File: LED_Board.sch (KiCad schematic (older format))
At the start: 26 parts, among them J1 Conn_01x06, J2 Conn_01x02, SW1 SW_Push, U1 PCA9531PW_LED_Driver_i2c

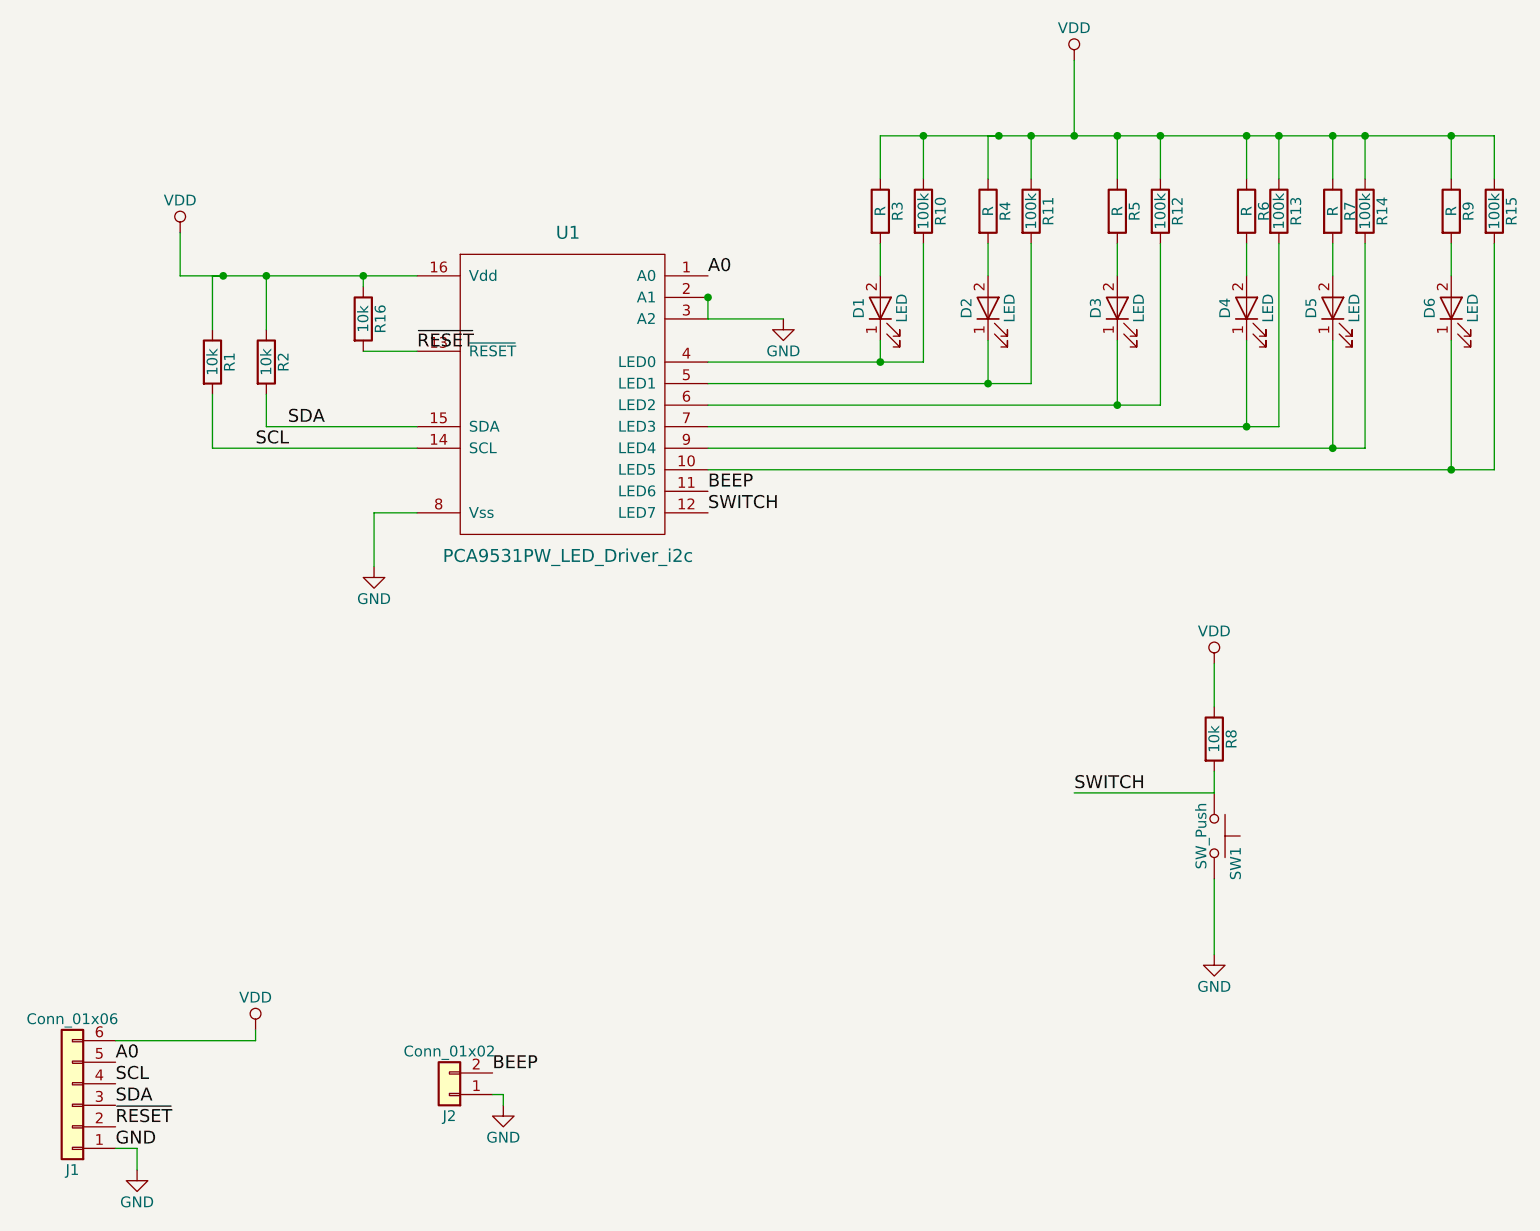
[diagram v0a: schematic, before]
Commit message: Arduino code able to read/write
Fixed a bug that stopped the code reading the status of the input pins.

Updated the PCB files based on the findings that I made during bring-up.
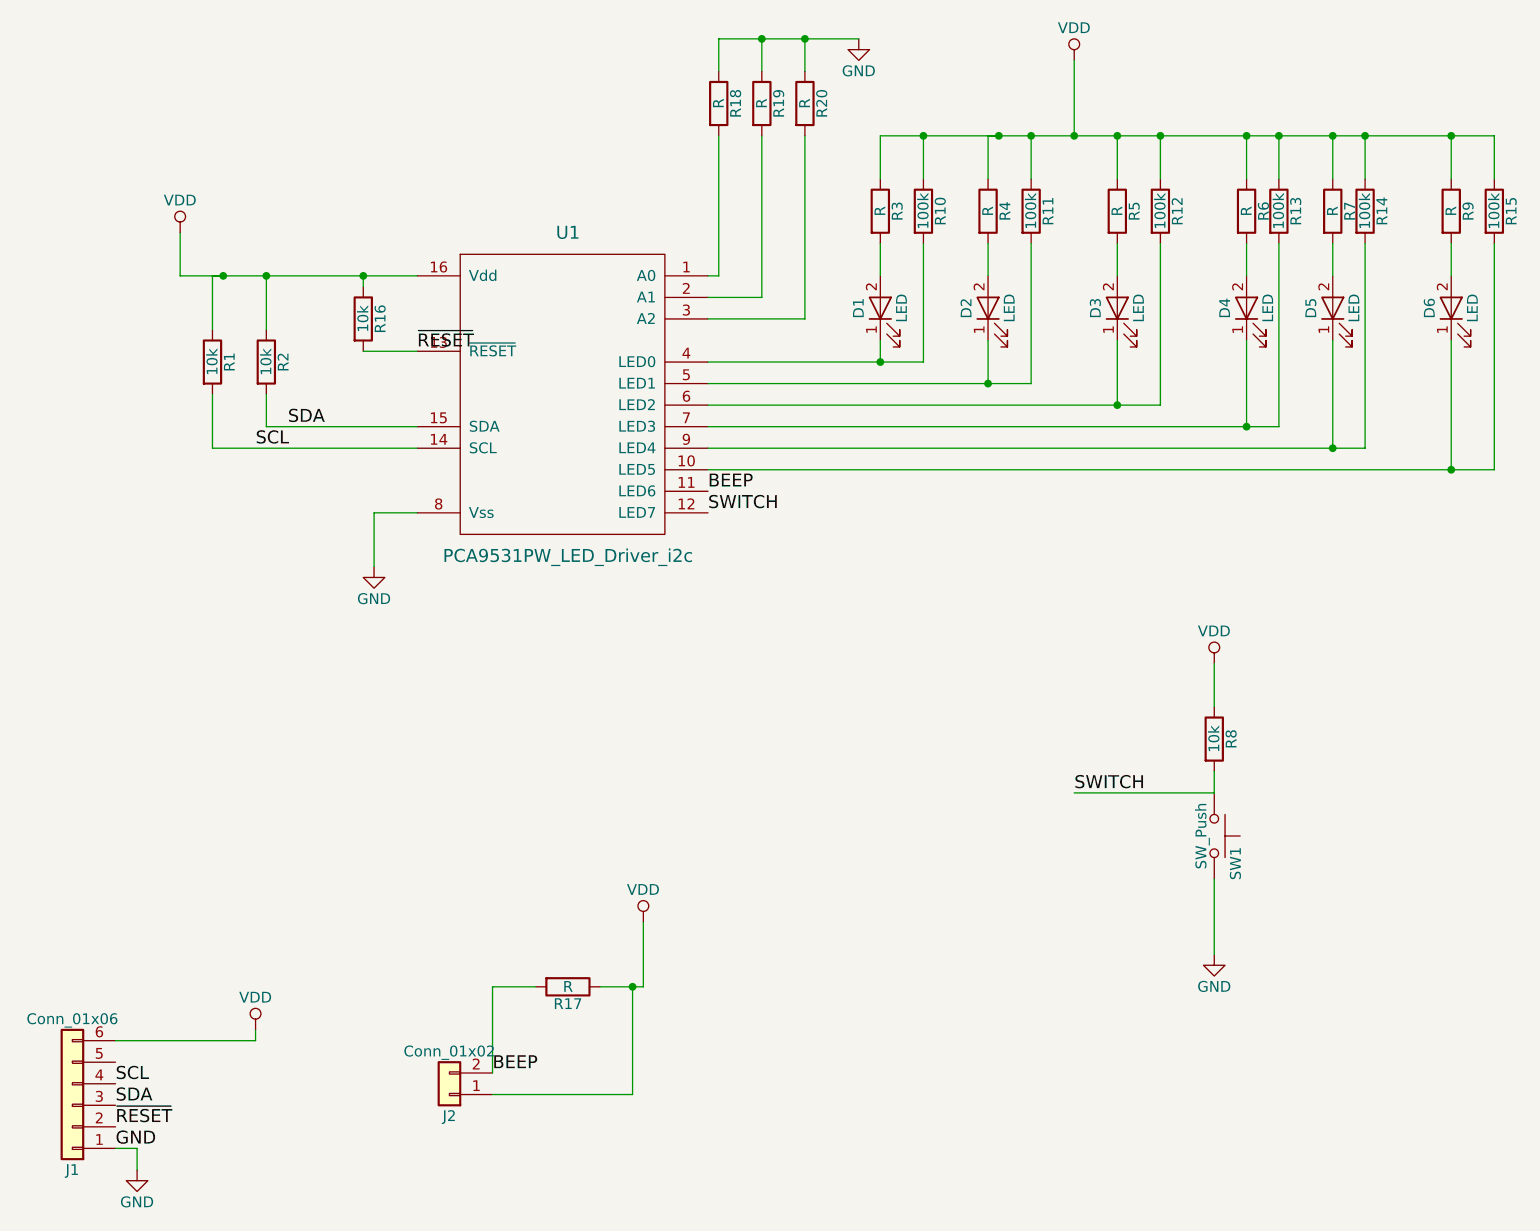
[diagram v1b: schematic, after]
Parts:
- added R17: R, Resistors_SMD:R_1206_HandSoldering, symbol R
- added R18, R19, R20: R, TJS-Kicad:R_1206_Jumper, symbol R
- SW1: footprint Buttons_Switches_THT:SW_TH_Tactile_Omron_B3F-10xx -> Buttons_Switches_THT:SW_PUSH_6mm
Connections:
- net BEEP: now also R17.2
- net GND: now also R18.1, R19.1, R20.1; no longer J2.1 (Pin_1), U1.2 (A1), U1.3 (A2)
- net VDD: now also J2.1 (Pin_1), R17.1
- net A0: no longer names the net of U1.1 (A0)
- net A0: now also R18.2; no longer J1.5 (Pin_5)
- new net: R19.2, U1.2 (A1)
- new net: R20.2, U1.3 (A2)
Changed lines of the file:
@@
 F 0 "SW1" H 7250 5050 50  0000 L CNN
 F 1 "SW_Push" H 7200 4890 50  0000 C CNN
-F 2 "Buttons_Switches_THT:SW_TH_Tactile_Omron_B3F-10xx" H 7200 5150 50  0001 C CNN
+F 2 "Buttons_Switches_THT:SW_PUSH_6mm" H 7200 5150 50  0001 C CNN
 F 3 "" H 7200 5150 50  0001 C CNN
 	1    7200 4950
@@
 F 3 "" H 7200 5500 50  0001 C CNN
 	1    7200 5500
-	1    0    0    -1
-$EndComp
-$Comp
-L GND #PWR07
-U 1 1 5A8C6805
-P 3900 6200
-F 0 "#PWR07" H 3900 5950 50  0001 C CNN
-F 1 "GND" H 3900 6050 50  0000 C CNN
-F 2 "" H 3900 6200 50  0001 C CNN
-F 3 "" H 3900 6200 50  0001 C CNN
-	1    3900 6200
 	1    0    0    -1
 $EndComp
@@
 	-1   0    0    1
 $EndComp
-Wire Wire Line
-	3850 6150 3900 6150
-Wire Wire Line
-	3900 6150 3900 6200
 Text Label 4850 3350 0    60   ~ 0
 BEEP
@@
 SWITCH
 $Comp
-L GND #PWR08
+L GND #PWR07
 U 1 1 5A8C80B3
-P 5200 2550
-F 0 "#PWR08" H 5200 2300 50  0001 C CNN
-F 1 "GND" H 5200 2400 50  0000 C CNN
-F 2 "" H 5200 2550 50  0001 C CNN
-F 3 "" H 5200 2550 50  0001 C CNN
-	1    5200 2550
-	1    0    0    -1
-$EndComp
-Wire Wire Line
-	4850 2550 5200 2550
-Connection ~ 4850 2450
+P 5550 1250
+F 0 "#PWR07" H 5550 1000 50  0001 C CNN
+F 1 "GND" H 5550 1100 50  0000 C CNN
+F 2 "" H 5550 1250 50  0001 C CNN
+F 3 "" H 5550 1250 50  0001 C CNN
+	1    5550 1250
+	1    0    0    -1
+$EndComp
 Text Label 3500 2700 0    60   ~ 0
 ~RESET
@@
 SCL
 $Comp
-L GND #PWR09
+L GND #PWR08
 U 1 1 5A8D6850
 P 2200 6500
-F 0 "#PWR09" H 2200 6250 50  0001 C CNN
+F 0 "#PWR08" H 2200 6250 50  0001 C CNN
 F 1 "GND" H 2200 6350 50  0000 C CNN
 F 2 "" H 2200 6500 50  0001 C CNN
@@
 $EndComp
 Wire Wire Line
-	4850 2450 4850 2550
-Text Label 4850 2350 0    60   ~ 0
-A0
-Text Label 2100 6000 0    60   ~ 0
-A0
-Wire Wire Line
 	4850 2750 5850 2750
 Connection ~ 5650 2750
@@
 Wire Wire Line
 	3500 2700 3250 2700
+$Comp
+L R R18
+U 1 1 5AA2825C
+P 4900 1550
+F 0 "R18" V 4980 1550 50  0000 C CNN
+F 1 "R" V 4900 1550 50  0000 C CNN
+F 2 "TJS-Kicad:R_1206_Jumper" V 4830 1550 50  0001 C CNN
+F 3 "" H 4900 1550 50  0001 C CNN
+	1    4900 1550
+	1    0    0    -1
+$EndComp
+$Comp
+L R R19
+U 1 1 5AA282EF
+P 5100 1550
+F 0 "R19" V 5180 1550 50  0000 C CNN
+F 1 "R" V 5100 1550 50  0000 C CNN
+F 2 "TJS-Kicad:R_1206_Jumper" V 5030 1550 50  0001 C CNN
+F 3 "" H 5100 1550 50  0001 C CNN
+	1    5100 1550
+	1    0    0    -1
+$EndComp
+$Comp
+L R R20
+U 1 1 5AA28357
+P 5300 1550
+F 0 "R20" V 5380 1550 50  0000 C CNN
+F 1 "R" V 5300 1550 50  0000 C CNN
+F 2 "TJS-Kicad:R_1206_Jumper" V 5230 1550 50  0001 C CNN
+F 3 "" H 5300 1550 50  0001 C CNN
+	1    5300 1550
+	1    0    0    -1
+$EndComp
+Wire Wire Line
+	4900 1250 5550 1250
+Wire Wire Line
+	5300 1250 5300 1400
+Wire Wire Line
+	5100 1400 5100 1250
+Connection ~ 5300 1250
+Wire Wire Line
+	4900 1400 4900 1250
+Connection ~ 5100 1250
+Wire Wire Line
+	4900 1700 4900 2350
+Wire Wire Line
+	4900 2350 4850 2350
+Wire Wire Line
+	5100 1700 5100 2450
+Wire Wire Line
+	5100 2450 4850 2450
+Wire Wire Line
+	5300 1700 5300 2550
+Wire Wire Line
+	5300 2550 4850 2550
+$Comp
+L VDD #PWR09
+U 1 1 5AA28F26
+P 4550 5350
+F 0 "#PWR09" H 4550 5200 50  0001 C CNN
+F 1 "VDD" H 4550 5500 50  0000 C CNN
+F 2 "" H 4550 5350 50  0001 C CNN
+F 3 "" H 4550 5350 50  0001 C CNN
+	1    4550 5350
+	1    0    0    -1
+$EndComp
+Wire Wire Line
+	4500 6150 3850 6150
+Wire Wire Line
+	4500 5650 4500 6150
+$Comp
+L R R17
+U 1 1 5AA29108
+P 4200 5650
+F 0 "R17" V 4280 5650 50  0000 C CNN
+F 1 "R" V 4200 5650 50  0000 C CNN
+F 2 "Resistors_SMD:R_1206_HandSoldering" V 4130 5650 50  0001 C CNN
+F 3 "" H 4200 5650 50  0001 C CNN
+	1    4200 5650
+	0    1    1    0
+$EndComp
+Wire Wire Line
+	4350 5650 4550 5650
+Wire Wire Line
+	4550 5650 4550 5350
+Connection ~ 4500 5650
+Wire Wire Line
+	4050 5650 3850 5650
+Wire Wire Line
+	3850 5650 3850 6050
 $EndSCHEMATC
